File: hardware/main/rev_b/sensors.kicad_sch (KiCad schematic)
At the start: 16 parts, among them U20 ICM-42688-P, U21 LSM6DSO32TR, U22 LPS22DFTR

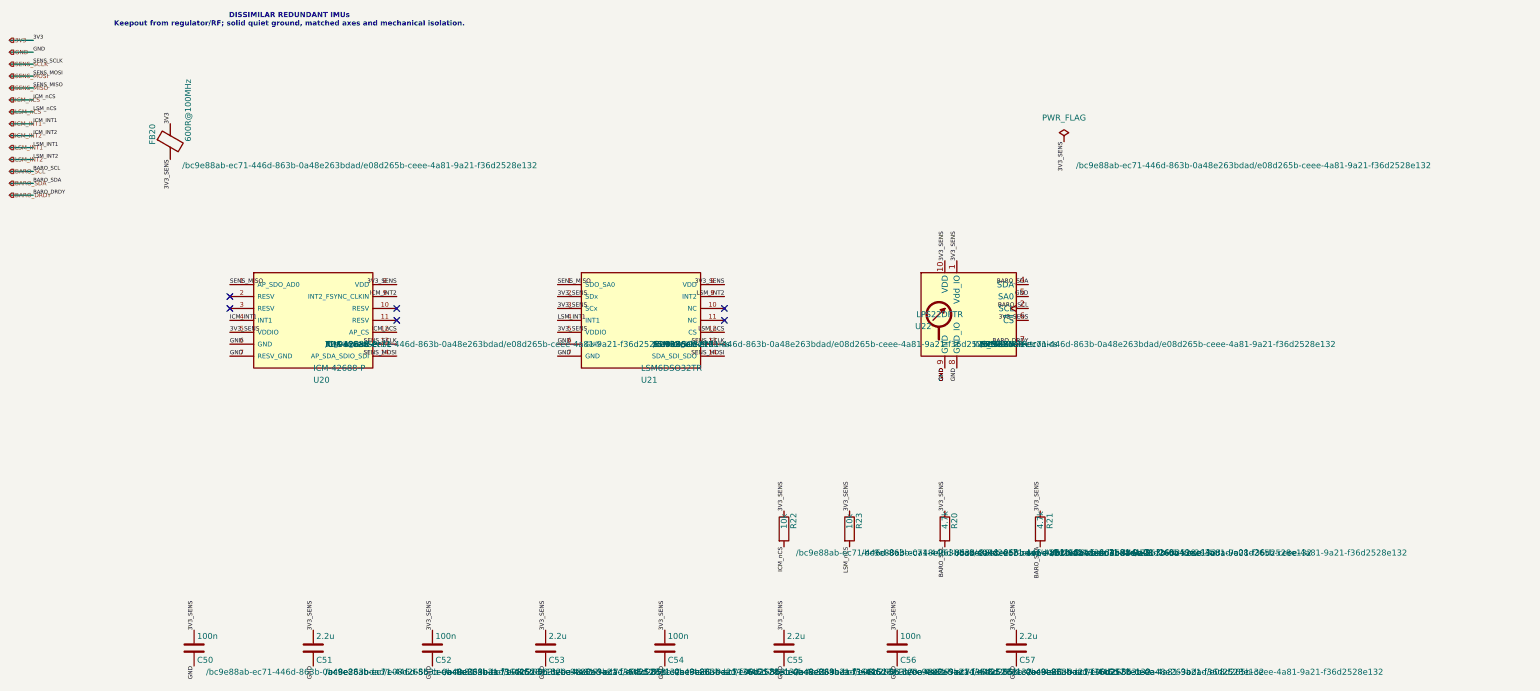
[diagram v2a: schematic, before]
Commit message: build: route and validate rev-b boards
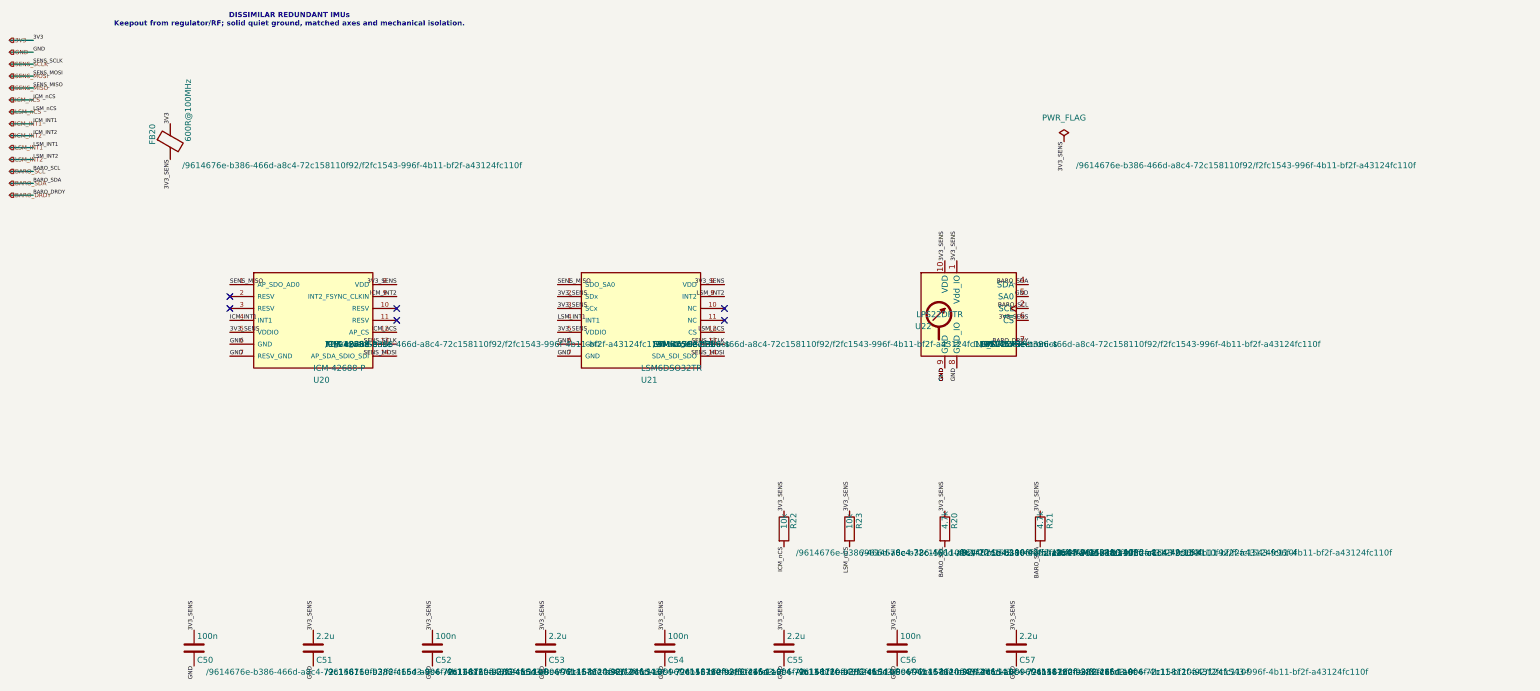
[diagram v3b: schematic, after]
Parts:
- C50, C51, C52, C53, C54, C55, C56, C57, FB20, R20, R21, R22, R23, U20, U21, U22: hierarchy_path /bc9e88ab-ec71-446d-863b-0a48e263bdad/e08d265b-ceee-4a81-9a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 -> /9614676e-b386-466d-a8c4-72c158110f92/f2fc1543-996f-4b11-bf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
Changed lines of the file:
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@@
 			)
 		)
-		(property "hierarchy_path" "/bc9e88ab-ec71-446d-863b-0a48e263bdad/e08d265b-ceee-4a81-9a21-f36d2528e132"
+		(property "hierarchy_path" "/9614676e-b386-466d-a8c4-72c158110f92/f2fc1543-996f-4b11-bf2f-a43124fc110f"
 			(at 57.15 46.9899 0)
 			(effects
@@
 		(instances
 			(project "main_rev_b"
-				(path "/bc9e88ab-ec71-446d-863b-0a48e263bdad/e08d265b-ceee-4a81-9a21-f36d2528e132"
+				(path "/9614676e-b386-466d-a8c4-72c158110f92/f2fc1543-996f-4b11-bf2f-a43124fc110f"
 					(reference "FB20")
 					(unit 1)
@@
 			)
 		)
-		(property "hierarchy_path" "/bc9e88ab-ec71-446d-863b-0a48e263bdad/e08d265b-ceee-4a81-9a21-f36d2528e132"
+		(property "hierarchy_path" "/9614676e-b386-466d-a8c4-72c158110f92/f2fc1543-996f-4b11-bf2f-a43124fc110f"
 			(at 87.63 85.0899 0)
 			(effects
@@
 		(instances
 			(project "main_rev_b"
-				(path "/bc9e88ab-ec71-446d-863b-0a48e263bdad/e08d265b-ceee-4a81-9a21-f36d2528e132"
+				(path "/9614676e-b386-466d-a8c4-72c158110f92/f2fc1543-996f-4b11-bf2f-a43124fc110f"
 					(reference "U20")
 					(unit 1)
@@
 			)
 		)
-		(property "hierarchy_path" "/bc9e88ab-ec71-446d-863b-0a48e263bdad/e08d265b-ceee-4a81-9a21-f36d2528e132"
+		(property "hierarchy_path" "/9614676e-b386-466d-a8c4-72c158110f92/f2fc1543-996f-4b11-bf2f-a43124fc110f"
 			(at 157.48 85.0899 0)
 			(effects
@@
 		(instances
 			(project "main_rev_b"
-				(path "/bc9e88ab-ec71-446d-863b-0a48e263bdad/e08d265b-ceee-4a81-9a21-f36d2528e132"
+				(path "/9614676e-b386-466d-a8c4-72c158110f92/f2fc1543-996f-4b11-bf2f-a43124fc110f"
 					(reference "U21")
 					(unit 1)
@@
 			)
 		)
-		(property "hierarchy_path" "/bc9e88ab-ec71-446d-863b-0a48e263bdad/e08d265b-ceee-4a81-9a21-f36d2528e132"
+		(property "hierarchy_path" "/9614676e-b386-466d-a8c4-72c158110f92/f2fc1543-996f-4b11-bf2f-a43124fc110f"
 			(at 227.33 85.0899 0)
 			(effects
@@
 		(instances
 			(project "main_rev_b"
-				(path "/bc9e88ab-ec71-446d-863b-0a48e263bdad/e08d265b-ceee-4a81-9a21-f36d2528e132"
+				(path "/9614676e-b386-466d-a8c4-72c158110f92/f2fc1543-996f-4b11-bf2f-a43124fc110f"
 					(reference "U22")
 					(unit 1)
@@
 			)
 		)
-		(property "hierarchy_path" "/bc9e88ab-ec71-446d-863b-0a48e263bdad/e08d265b-ceee-4a81-9a21-f36d2528e132"
+		(property "hierarchy_path" "/9614676e-b386-466d-a8c4-72c158110f92/f2fc1543-996f-4b11-bf2f-a43124fc110f"
 			(at 222.25 129.5399 0)
 			(effects
@@
 		(instances
 			(project "main_rev_b"
-				(path "/bc9e88ab-ec71-446d-863b-0a48e263bdad/e08d265b-ceee-4a81-9a21-f36d2528e132"
+				(path "/9614676e-b386-466d-a8c4-72c158110f92/f2fc1543-996f-4b11-bf2f-a43124fc110f"
 					(reference "R20")
 					(unit 1)
@@
 			)
 		)
-		(property "hierarchy_path" "/bc9e88ab-ec71-446d-863b-0a48e263bdad/e08d265b-ceee-4a81-9a21-f36d2528e132"
+		(property "hierarchy_path" "/9614676e-b386-466d-a8c4-72c158110f92/f2fc1543-996f-4b11-bf2f-a43124fc110f"
 			(at 242.57 129.5399 0)
 			(effects
@@
 		(instances
 			(project "main_rev_b"
-				(path "/bc9e88ab-ec71-446d-863b-0a48e263bdad/e08d265b-ceee-4a81-9a21-f36d2528e132"
+				(path "/9614676e-b386-466d-a8c4-72c158110f92/f2fc1543-996f-4b11-bf2f-a43124fc110f"
 					(reference "R21")
 					(unit 1)
@@
 			)
 		)
-		(property "hierarchy_path" "/bc9e88ab-ec71-446d-863b-0a48e263bdad/e08d265b-ceee-4a81-9a21-f36d2528e132"
+		(property "hierarchy_path" "/9614676e-b386-466d-a8c4-72c158110f92/f2fc1543-996f-4b11-bf2f-a43124fc110f"
 			(at 187.96 129.5399 0)
 			(effects
@@
 		(instances
 			(project "main_rev_b"
-				(path "/bc9e88ab-ec71-446d-863b-0a48e263bdad/e08d265b-ceee-4a81-9a21-f36d2528e132"
+				(path "/9614676e-b386-466d-a8c4-72c158110f92/f2fc1543-996f-4b11-bf2f-a43124fc110f"
 					(reference "R22")
 					(unit 1)
@@
 			)
 		)
-		(property "hierarchy_path" "/bc9e88ab-ec71-446d-863b-0a48e263bdad/e08d265b-ceee-4a81-9a21-f36d2528e132"
+		(property "hierarchy_path" "/9614676e-b386-466d-a8c4-72c158110f92/f2fc1543-996f-4b11-bf2f-a43124fc110f"
 			(at 201.93 129.5399 0)
 			(effects
@@
 		(instances
 			(project "main_rev_b"
-				(path "/bc9e88ab-ec71-446d-863b-0a48e263bdad/e08d265b-ceee-4a81-9a21-f36d2528e132"
+				(path "/9614676e-b386-466d-a8c4-72c158110f92/f2fc1543-996f-4b11-bf2f-a43124fc110f"
 					(reference "R23")
 					(unit 1)
@@
 			)
 		)
-		(property "hierarchy_path" "/bc9e88ab-ec71-446d-863b-0a48e263bdad/e08d265b-ceee-4a81-9a21-f36d2528e132"
+		(property "hierarchy_path" "/9614676e-b386-466d-a8c4-72c158110f92/f2fc1543-996f-4b11-bf2f-a43124fc110f"
 			(at 62.23 154.9399 0)
 			(effects
@@
 		(instances
 			(project "main_rev_b"
-				(path "/bc9e88ab-ec71-446d-863b-0a48e263bdad/e08d265b-ceee-4a81-9a21-f36d2528e132"
+				(path "/9614676e-b386-466d-a8c4-72c158110f92/f2fc1543-996f-4b11-bf2f-a43124fc110f"
 					(reference "C50")
 					(unit 1)
@@
 			)
 		)
-		(property "hierarchy_path" "/bc9e88ab-ec71-446d-863b-0a48e263bdad/e08d265b-ceee-4a81-9a21-f36d2528e132"
+		(property "hierarchy_path" "/9614676e-b386-466d-a8c4-72c158110f92/f2fc1543-996f-4b11-bf2f-a43124fc110f"
 			(at 87.63 154.9399 0)
 			(effects
@@
 		(instances
 			(project "main_rev_b"
-				(path "/bc9e88ab-ec71-446d-863b-0a48e263bdad/e08d265b-ceee-4a81-9a21-f36d2528e132"
+				(path "/9614676e-b386-466d-a8c4-72c158110f92/f2fc1543-996f-4b11-bf2f-a43124fc110f"
 					(reference "C51")
 					(unit 1)
@@
 			)
 		)
-		(property "hierarchy_path" "/bc9e88ab-ec71-446d-863b-0a48e263bdad/e08d265b-ceee-4a81-9a21-f36d2528e132"
+		(property "hierarchy_path" "/9614676e-b386-466d-a8c4-72c158110f92/f2fc1543-996f-4b11-bf2f-a43124fc110f"
 			(at 113.03 154.9399 0)
 			(effects
@@
 		(instances
 			(project "main_rev_b"
-				(path "/bc9e88ab-ec71-446d-863b-0a48e263bdad/e08d265b-ceee-4a81-9a21-f36d2528e132"
+				(path "/9614676e-b386-466d-a8c4-72c158110f92/f2fc1543-996f-4b11-bf2f-a43124fc110f"
 					(reference "C52")
 					(unit 1)
@@
 			)
 		)
-		(property "hierarchy_path" "/bc9e88ab-ec71-446d-863b-0a48e263bdad/e08d265b-ceee-4a81-9a21-f36d2528e132"
+		(property "hierarchy_path" "/9614676e-b386-466d-a8c4-72c158110f92/f2fc1543-996f-4b11-bf2f-a43124fc110f"
 			(at 137.16 154.9399 0)
 			(effects
@@
 		(instances
 			(project "main_rev_b"
-				(path "/bc9e88ab-ec71-446d-863b-0a48e263bdad/e08d265b-ceee-4a81-9a21-f36d2528e132"
+				(path "/9614676e-b386-466d-a8c4-72c158110f92/f2fc1543-996f-4b11-bf2f-a43124fc110f"
 					(reference "C53")
 					(unit 1)
@@
 			)
 		)
-		(property "hierarchy_path" "/bc9e88ab-ec71-446d-863b-0a48e263bdad/e08d265b-ceee-4a81-9a21-f36d2528e132"
+		(property "hierarchy_path" "/9614676e-b386-466d-a8c4-72c158110f92/f2fc1543-996f-4b11-bf2f-a43124fc110f"
 			(at 162.56 154.9399 0)
 			(effects
@@
 		(instances
 			(project "main_rev_b"
-				(path "/bc9e88ab-ec71-446d-863b-0a48e263bdad/e08d265b-ceee-4a81-9a21-f36d2528e132"
+				(path "/9614676e-b386-466d-a8c4-72c158110f92/f2fc1543-996f-4b11-bf2f-a43124fc110f"
 					(reference "C54")
 					(unit 1)
@@
 			)
 		)
-		(property "hierarchy_path" "/bc9e88ab-ec71-446d-863b-0a48e263bdad/e08d265b-ceee-4a81-9a21-f36d2528e132"
+		(property "hierarchy_path" "/9614676e-b386-466d-a8c4-72c158110f92/f2fc1543-996f-4b11-bf2f-a43124fc110f"
 			(at 187.96 154.9399 0)
 			(effects
@@
 		(instances
 			(project "main_rev_b"
-				(path "/bc9e88ab-ec71-446d-863b-0a48e263bdad/e08d265b-ceee-4a81-9a21-f36d2528e132"
+				(path "/9614676e-b386-466d-a8c4-72c158110f92/f2fc1543-996f-4b11-bf2f-a43124fc110f"
 					(reference "C55")
 					(unit 1)
@@
 			)
 		)
-		(property "hierarchy_path" "/bc9e88ab-ec71-446d-863b-0a48e263bdad/e08d265b-ceee-4a81-9a21-f36d2528e132"
+		(property "hierarchy_path" "/9614676e-b386-466d-a8c4-72c158110f92/f2fc1543-996f-4b11-bf2f-a43124fc110f"
 			(at 212.09 154.9399 0)
 			(effects
@@
 		(instances
 			(project "main_rev_b"
-				(path "/bc9e88ab-ec71-446d-863b-0a48e263bdad/e08d265b-ceee-4a81-9a21-f36d2528e132"
+				(path "/9614676e-b386-466d-a8c4-72c158110f92/f2fc1543-996f-4b11-bf2f-a43124fc110f"
 					(reference "C56")
 					(unit 1)
@@
 			)
 		)
-		(property "hierarchy_path" "/bc9e88ab-ec71-446d-863b-0a48e263bdad/e08d265b-ceee-4a81-9a21-f36d2528e132"
+		(property "hierarchy_path" "/9614676e-b386-466d-a8c4-72c158110f92/f2fc1543-996f-4b11-bf2f-a43124fc110f"
 			(at 237.49 154.9399 0)
 			(effects
@@
 		(instances
 			(project "main_rev_b"
-				(path "/bc9e88ab-ec71-446d-863b-0a48e263bdad/e08d265b-ceee-4a81-9a21-f36d2528e132"
+				(path "/9614676e-b386-466d-a8c4-72c158110f92/f2fc1543-996f-4b11-bf2f-a43124fc110f"
 					(reference "C57")
 					(unit 1)
@@
 			)
 		)
-		(property "hierarchy_path" "/bc9e88ab-ec71-446d-863b-0a48e263bdad/e08d265b-ceee-4a81-9a21-f36d2528e132"
+		(property "hierarchy_path" "/9614676e-b386-466d-a8c4-72c158110f92/f2fc1543-996f-4b11-bf2f-a43124fc110f"
 			(at 247.65 46.9899 0)
 			(effects
@@
 		(instances
 			(project "main_rev_b"
-				(path "/bc9e88ab-ec71-446d-863b-0a48e263bdad/e08d265b-ceee-4a81-9a21-f36d2528e132"
+				(path "/9614676e-b386-466d-a8c4-72c158110f92/f2fc1543-996f-4b11-bf2f-a43124fc110f"
 					(reference "#FLG20")
 					(unit 1)
